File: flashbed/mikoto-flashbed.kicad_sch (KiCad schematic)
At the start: 49 parts, among them J1 Conn_01x01, J2 Conn_01x01, J3 Conn_01x01, J4 Conn_01x01, J5 Conn_01x01, J6 Conn_01x01, J7 Conn_01x05, SW1 TVBP06, U1 ProMicro_2

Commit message: update flashbed and add gerbers
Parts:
- removed D10, D11, D12, D13, D14, D15, D16, D17, D18, D19, D2, D20, D3, D4, D5, D6, D7, D8, D9: LED_Small, LED_SMD:LED_1206_3216Metric_Pad1.42x1.75mm_HandSolder, symbol Device:LED_Small
- removed R10, R11, R12, R13, R14, R15, R16, R17, R18, R19, R2, R20, R3, R4, R5, R6, R7, R8, R9: 2.2k, Resistor_SMD:R_0805_2012Metric_Pad1.15x1.40mm_HandSolder, symbol Device:R_Small
- added J8: Conn_01x01, Connector_PinHeader_2.54mm:PinHeader_1x01_P2.54mm_Vertical, symbol Connector_Generic:Conn_01x01
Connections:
- net EXT_5V: no longer names the net of J5.1 (Pin_1)
- net EXT_VCC: no longer names the net of U1.21 (VCC)
- net P0.02: no longer names the net of U1.18 (A1(PF6))
- net P0.06: no longer names the net of U1.1 (TX(PD3))
- net P0.08: no longer names the net of U1.2 (RX(PD2))
- net P0.09: no longer names the net of D1.2 (A)
- net P0.09: now also J8.1 (Pin_1); no longer U1.13 (D10(PB6))
- net P0.10: no longer names the net of U1.14 (D16(PB2))
- net P0.11: no longer names the net of U1.20 (A3(PF4))
- net P0.17: no longer names the net of U1.5 (SDA(PD1))
- net P0.20: no longer names the net of U1.6 (SCL(PD0))
- net P0.22: no longer names the net of U1.7 (D4(PD4))
- net P0.24: no longer names the net of U1.8 (D5(PC6))
- net P0.25: no longer names the net of U1.19 (A2(PF5))
- net P0.31: no longer names the net of U1.10 (D7(PE6))
- net P1.00: no longer names the net of U1.9 (D6(PD7))
- net P1.04: no longer names the net of U1.11 (D8(PB4))
- net P1.06: no longer names the net of U1.12 (D9(PB5))
- net P1.11: no longer names the net of U1.15 (D14(PB3))
- net P1.13: no longer names the net of U1.16 (D15(PB1))
- net P1.15: no longer names the net of U1.17 (A0(PF7))
- net VBAT: no longer names the net of U1.24 (RAW)
- net VBUS: no longer names the net of J6.1 (Pin_1)
- no-connect marks 1 -> 23
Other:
- moved on the sheet: D1, J1, J2, J3, J4, R1

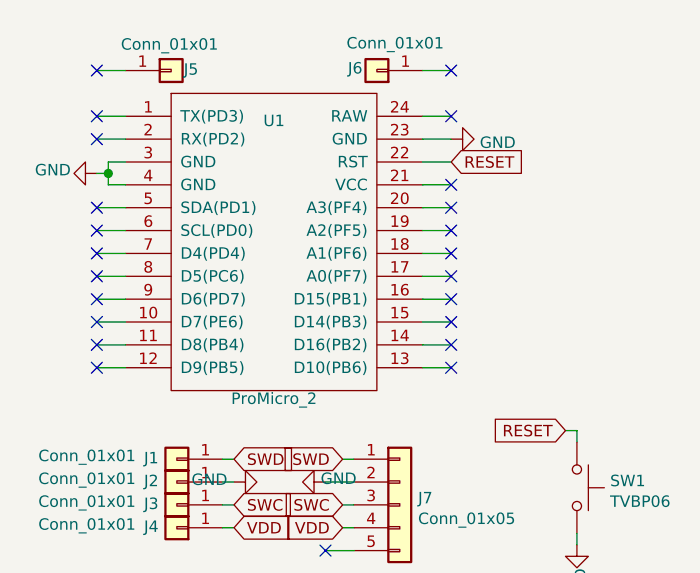
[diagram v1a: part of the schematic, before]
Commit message: rev 5.11
1. move thermal vias for bq24075 to not be literally under the paste
2. reduce the EP paste for the nrf52 (and place the vias between the
   paste islands)
3. remove all silks for passives because it's ugly
4. fix the incorrect pin labelling (since we switched P0.06 to P0.04)
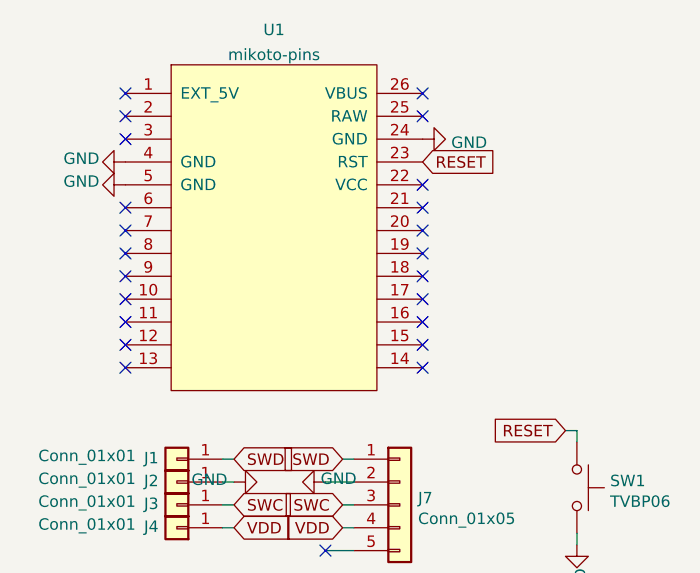
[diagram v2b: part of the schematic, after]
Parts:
- removed J5, J6: Conn_01x01, footprints:1pin_conn, symbol Connector_Generic:Conn_01x01
- removed U1: ProMicro_2, footprints:akami-pins, symbol mikoto:ProMicro_2
- added U1: mikoto-pins, footprints:mikoto-pins, symbol mikoto:mikoto-pins
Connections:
- net GND: now also U1.24 (GND), U1.4 (GND), U1.5 (GND)
- net RESET: now also U1.23 (RST)

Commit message: update flashbed
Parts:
- removed J8: Conn_01x01, Connector_PinHeader_2.54mm:PinHeader_1x01_P2.54mm_Vertical, symbol Connector_Generic:Conn_01x01
- added D10, D11, D12, D13, D14, D15, D16, D17, D18, D19, D2, D20, D21, D3, D4, D5, D6, D7, D8, D9: LED_Small, footprints:LED_1206_3216M_Castellated-nosilk, symbol Device:LED_Small
- added R10, R11, R12, R13, R14, R15, R16, R17, R18, R19, R2, R20, R21, R3, R4, R5, R6, R7, R8, R9: 2.2k, Resistor_SMD:R_0805_2012Metric_Pad1.15x1.40mm_HandSolder, symbol Device:R_Small
- D1: footprint LED_SMD:LED_1206_3216Metric_Pad1.42x1.75mm_HandSolder -> footprints:LED_1206_3216M_Castellated-nosilk
- U1: footprint footprints:mikoto-pins -> footprints:mikoto-pins-bigger-holes
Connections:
- net GND: now also D1.1 (K), D10.1 (K), D11.1 (K), D12.1 (K), D13.1 (K), D14.1 (K), D15.1 (K), D16.1 (K), D17.1 (K), D18.1 (K), D19.1 (K), D2.1 (K), D20.1 (K), D21.1 (K), D3.1 (K), D4.1 (K), D5.1 (K), D6.1 (K), D7.1 (K), D8.1 (K), D9.1 (K); no longer R1.2
- net EXT_5V: now reaches U1.1 (EXT_5V)
- net EXT_5V: now also R1.1
- net P1.00: now reaches U1.10
- net P1.00: now also R8.1
- net P1.02: now reaches U1.11
- net P1.02: now also R9.1
- net P1.04: now reaches U1.12
- net P1.04: now also R10.1
- net P1.06: now reaches U1.13
- net P1.06: now also R11.1
- net P0.09: now reaches U1.14
- net P0.09: now also R12.1
- net P0.10: now reaches U1.15
- net P0.10: now also R13.1
- net P1.11: now reaches U1.16
- net P1.11: now also R14.1
- net P0.02: now reaches U1.17
- net P0.02: now also R15.1
- net P0.29: now reaches U1.18
- net P0.29: now also R16.1
- net P0.31: now reaches U1.19
- net P0.31: now also R17.1
- net P0.08: now reaches U1.2
- net P0.08: now also R2.1
- net P0.25: now reaches U1.20
- net P0.25: now also R18.1
- net P0.11: now reaches U1.21
- net P0.11: now also R19.1
- net EXT_VCC: now reaches U1.22 (VCC)
- net EXT_VCC: now also R20.1
- net VBAT: now reaches U1.25 (RAW)
- net VBUS: now reaches U1.26 (VBUS)
- net VBUS: now also R21.1
- net P0.04: now reaches U1.3
- net P0.04: now also R3.1
- net P0.17: now reaches U1.6
- net P0.17: now also R4.1
- net P0.20: now reaches U1.7
- net P0.20: now also R5.1
- net P0.22: now reaches U1.8
- net P0.22: now also R6.1
- net P0.24: now reaches U1.9
- net P0.24: now also R7.1
- net at D1.2 (A): now also R1.2
- new net: D10.2 (A), R10.2
- new net: D16.2 (A), R16.2
- new net: D11.2 (A), R11.2
- new net: D4.2 (A), R4.2
- new net: D12.2 (A), R12.2
- new net: D14.2 (A), R14.2
- new net: D3.2 (A), R3.2
- new net: D7.2 (A), R7.2
- new net: D2.2 (A), R2.2
- new net: D18.2 (A), R18.2
- new net: D5.2 (A), R5.2
- new net: D6.2 (A), R6.2
- new net: D15.2 (A), R15.2
- new net: D17.2 (A), R17.2
- new net: D13.2 (A), R13.2
- new net: D21.2 (A), R21.2
- new net: D8.2 (A), R8.2
- new net: D20.2 (A), R20.2
- new net: D9.2 (A), R9.2
- new net: D19.2 (A), R19.2
- no-connect marks 23 -> 1
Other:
- moved on the sheet: R1

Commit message: some nonsense with the flashbed
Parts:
- added R22, R23, R24, R25, R26, R27, R28, R29: R_Small, Resistor_SMD:R_0201_0603Metric, symbol Device:R_Small
- added TP1, TP2, TP3, TP4, TP5, TP6, TP7, TP8: TestPoint, footprints:TestPoint_Pad_D1.0mm-nosilk, symbol Connector:TestPoint
- J7: footprint Connector_PinHeader_2.54mm:PinHeader_1x05_P2.54mm_Vertical -> Connector_PinHeader_2.54mm:PinHeader_1x05_P2.54mm_Horizontal
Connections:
- net EXT_5V: now also R22.2, TP1.1
- net GND: now also J7.4 (Pin_4), R29.1; no longer J7.2 (Pin_2)
- net SWD: now also J7.5 (Pin_5); no longer J7.1 (Pin_1)
- net VDD: now also J7.2 (Pin_2); no longer J7.4 (Pin_4)
- new net: R22.1, R23.2, TP2.1
- new net: R25.1, R26.2, TP5.1
- new net: R27.1, R28.2, TP7.1
- new net: R28.1, R29.2, TP8.1
- new net: R24.1, R25.2, TP4.1
- new net: R23.1, R24.2, TP3.1
- new net: R26.1, R27.2, TP6.1
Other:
- moved on the sheet: D1, D10, D11, D12, D13, D14, D15, D16, D17, D18, D19, D2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

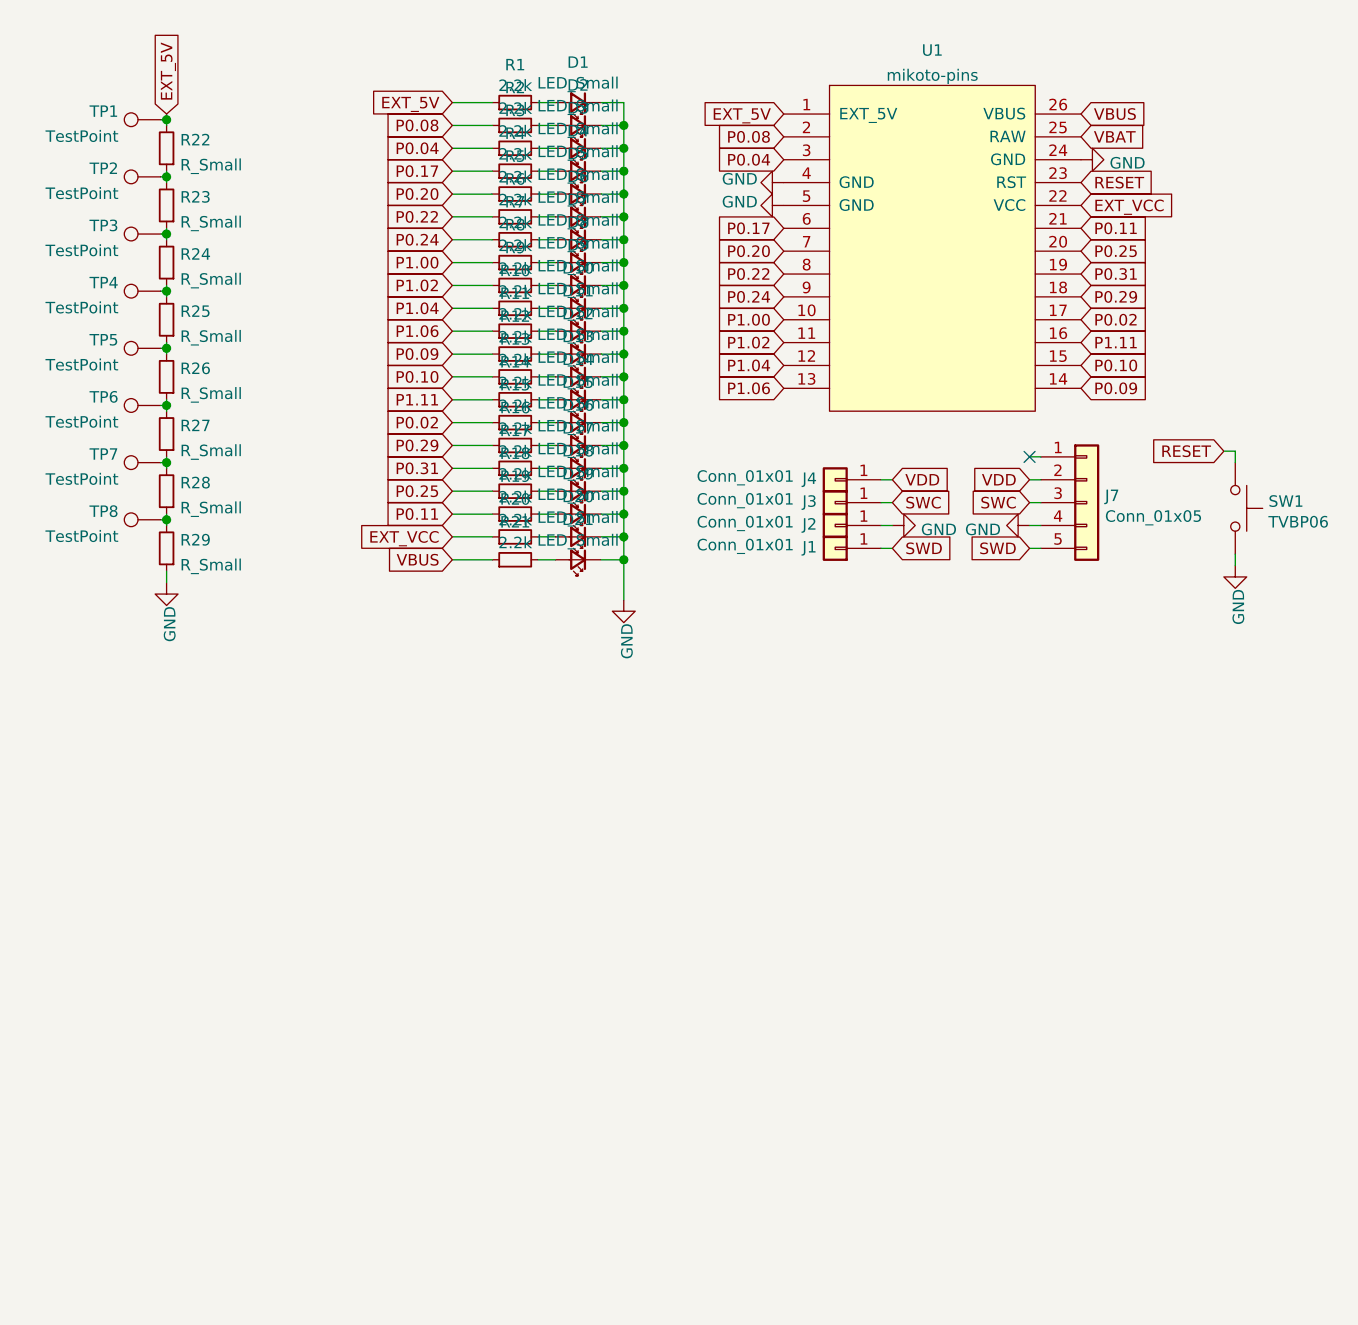
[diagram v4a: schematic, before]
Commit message: update flashbed for new underside pad placement
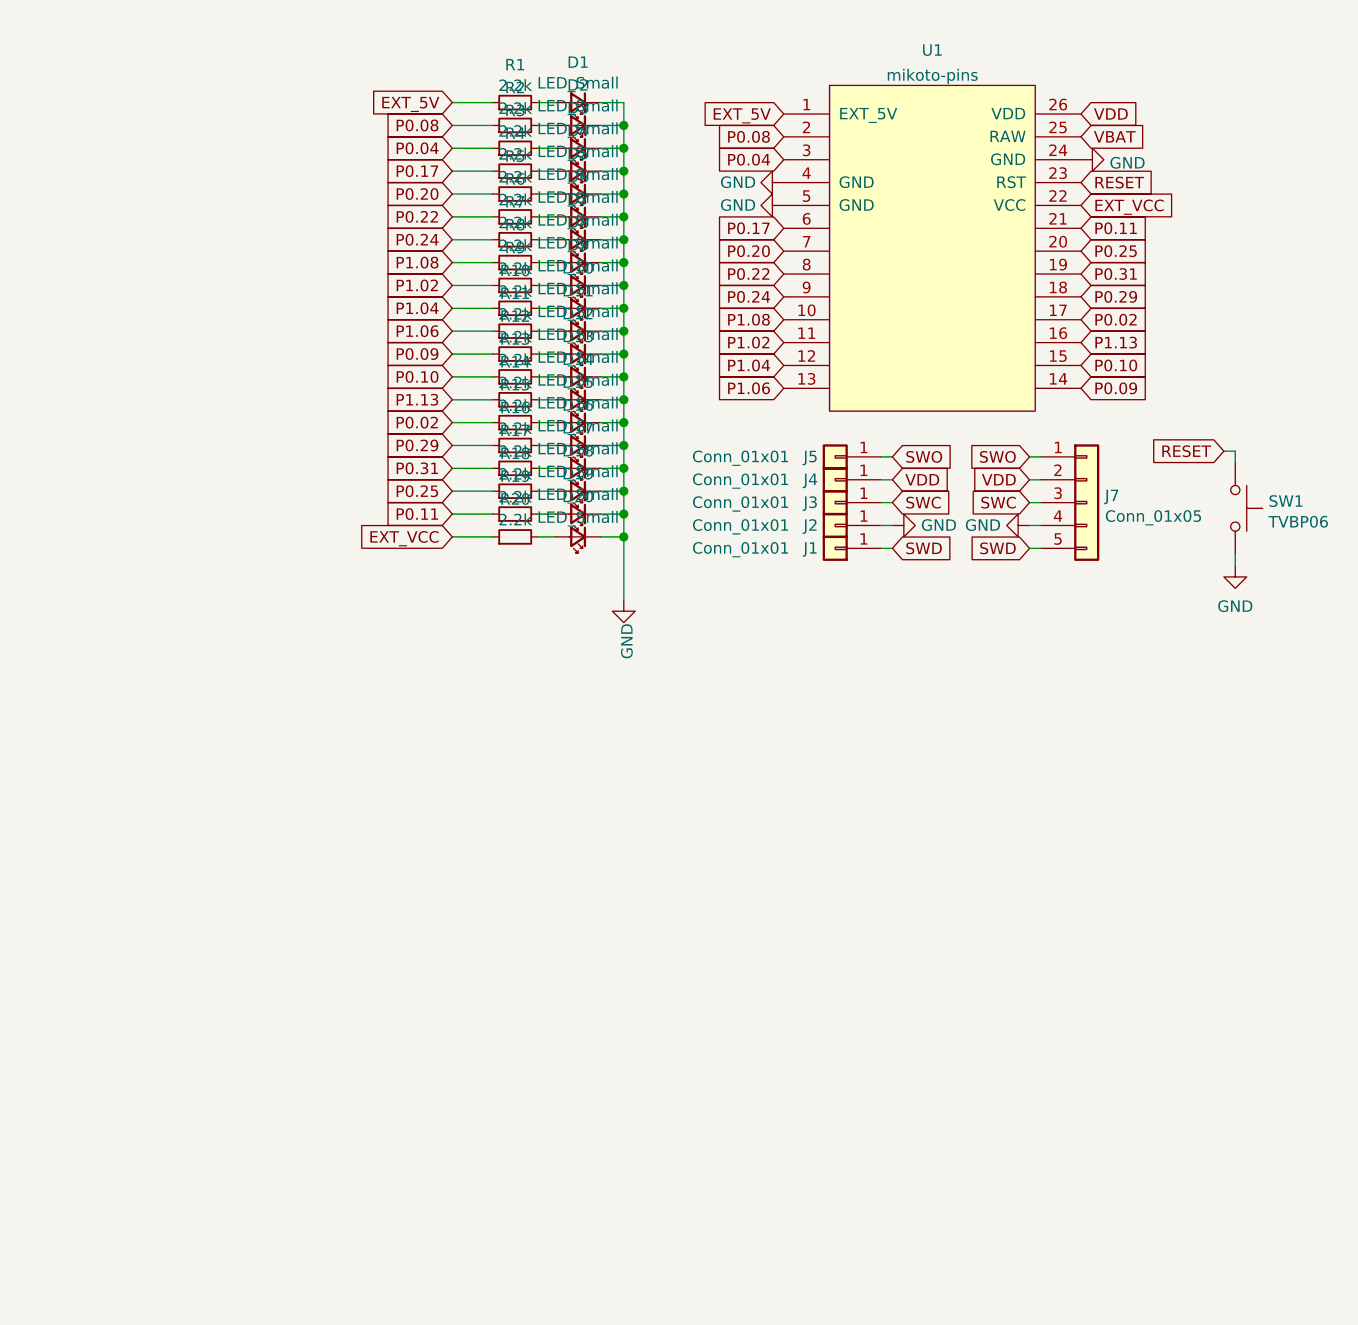
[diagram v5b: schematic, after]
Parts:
- removed D21: LED_Small, footprints:LED_1206_3216M_Castellated-nosilk, symbol Device:LED_Small
- removed R21: 2.2k, Resistor_SMD:R_0805_2012Metric_Pad1.15x1.40mm_HandSolder, symbol Device:R_Small
- removed R22, R23, R24, R25, R26, R27, R28, R29: R_Small, Resistor_SMD:R_0201_0603Metric, symbol Device:R_Small
- removed TP1, TP2, TP3, TP4, TP5, TP6, TP7, TP8: TestPoint, footprints:TestPoint_Pad_D1.0mm-nosilk, symbol Connector:TestPoint
- added J5: Conn_01x01, TestPoint:TestPoint_THTPad_D2.0mm_Drill1.0mm, symbol Connector_Generic:Conn_01x01
- U1: footprint footprints:mikoto-pins-bigger-holes -> footprints:mikoto-pins
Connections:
- net VBUS is gone; now on net VDD: U1.26 (VDD)
- net SWO: now reaches J7.1 (Pin_1)
- net SWO: now also J5.1 (Pin_1)
- net P1.00 renamed P1.08
- net P1.11 renamed P1.13
- no-connect marks 1 -> 0
